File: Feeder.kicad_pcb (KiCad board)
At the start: 4 copper layers, 91 x 85 mm, 171 parts, among them J101 Conn_02x03_Odd_Even, J102 Conn_01x03_Pin, Q201 2N7002, Q301 2N7002, Q401 2N7002, Q501 2N7002, Q901 BC857BS, Q902 AO3401A, Q903 BC857BS, Q904 AO3401A, U101 XBLW 24C02S(XBLW), U201 CMP6793RE, U301 CMP6793RE, U401 LM5169PDDAR, U501 LM5169PDDAR, U601 TPS562202, U701 TPS562202, U801 CMP6793RE

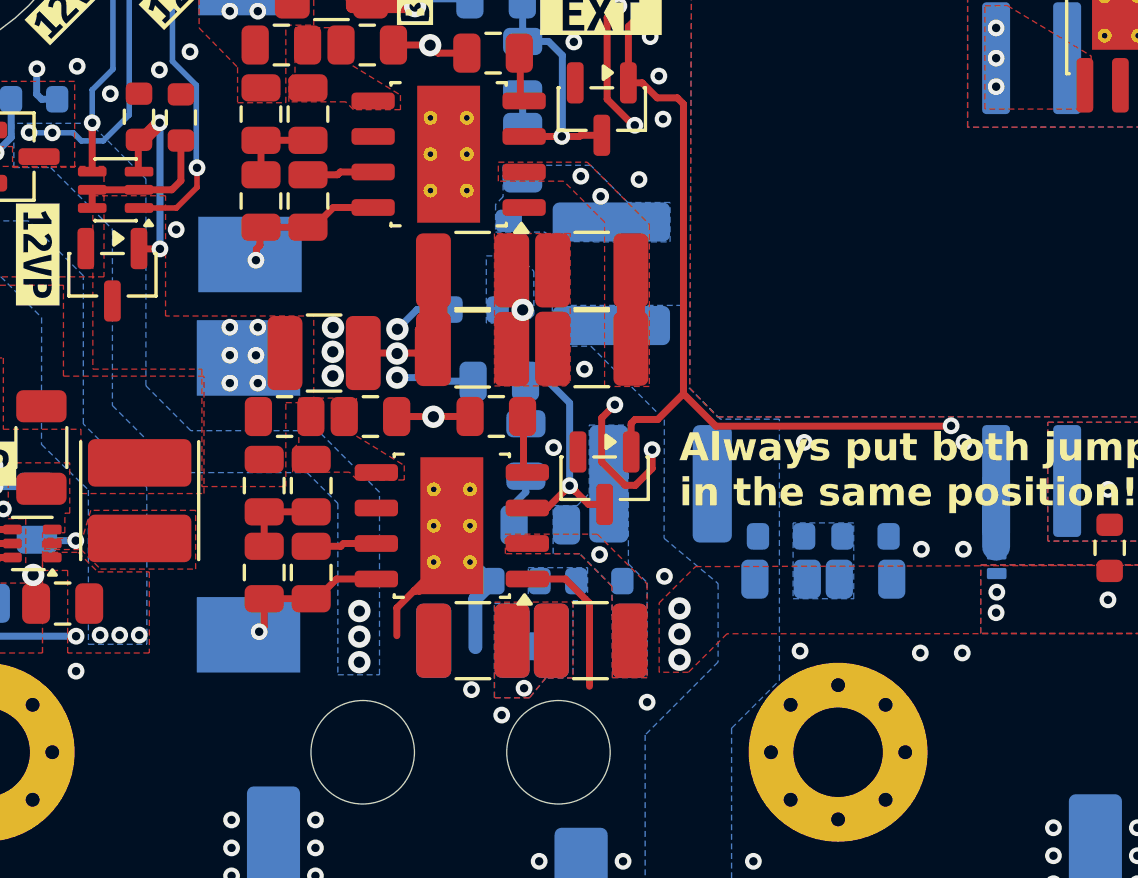
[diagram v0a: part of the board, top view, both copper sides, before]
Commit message: Updated the DRC rules so it now checks correctly B4 and A6 IPC2221 rules
Signed-off-by: Jean Alinei <jean.alinei@owntech.org>
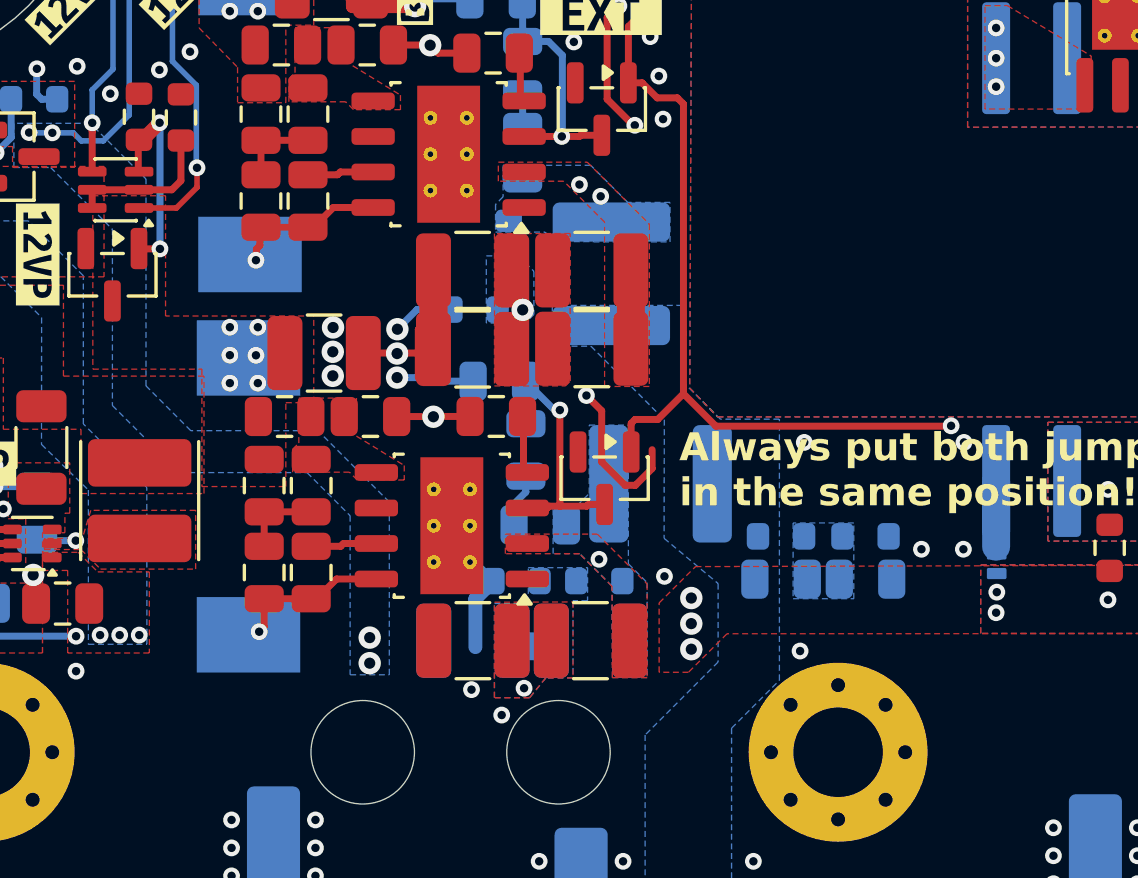
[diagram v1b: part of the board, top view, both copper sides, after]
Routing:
- net PGND: track 79.8 -> 69.0 mm, vias 165 -> 157
- net /12V_DIGI_TO_POWER: vias 14 -> 13

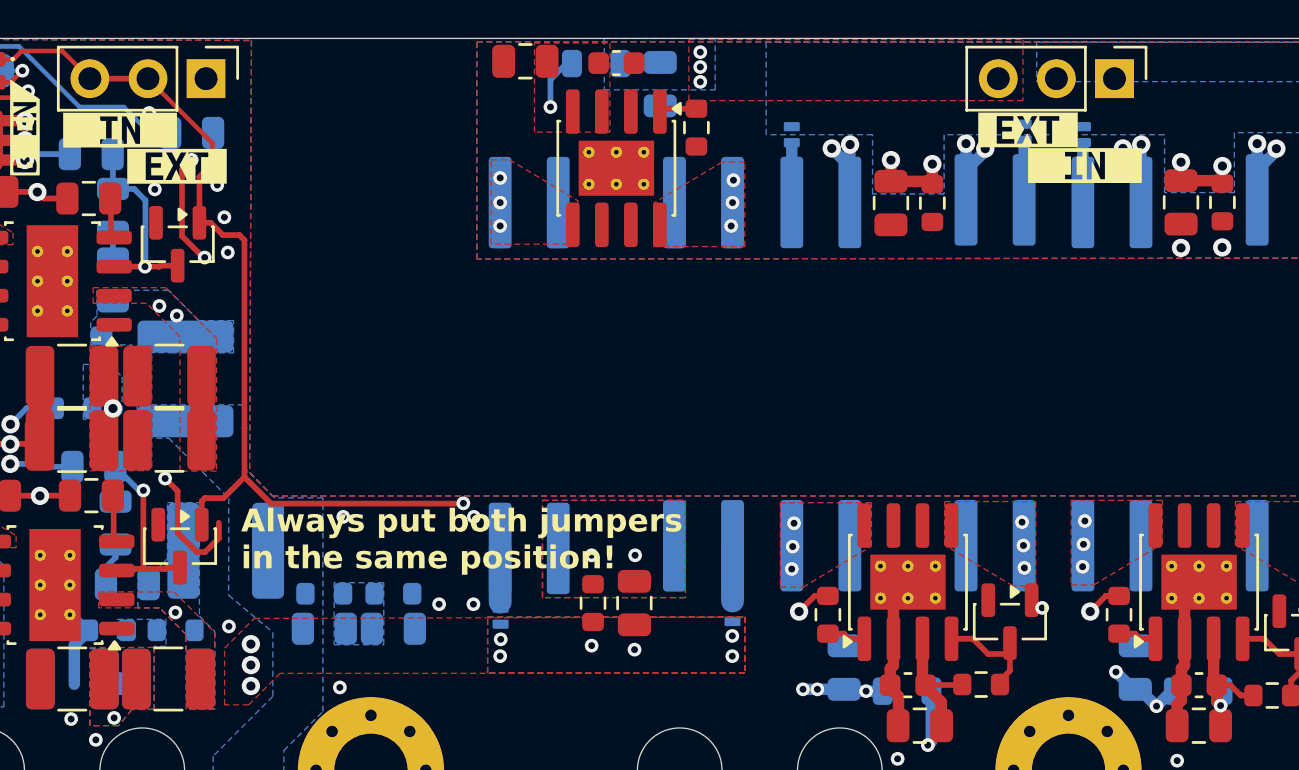
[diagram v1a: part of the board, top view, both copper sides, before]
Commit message: added y cap and changed the inductor value, added simulator of pi filter
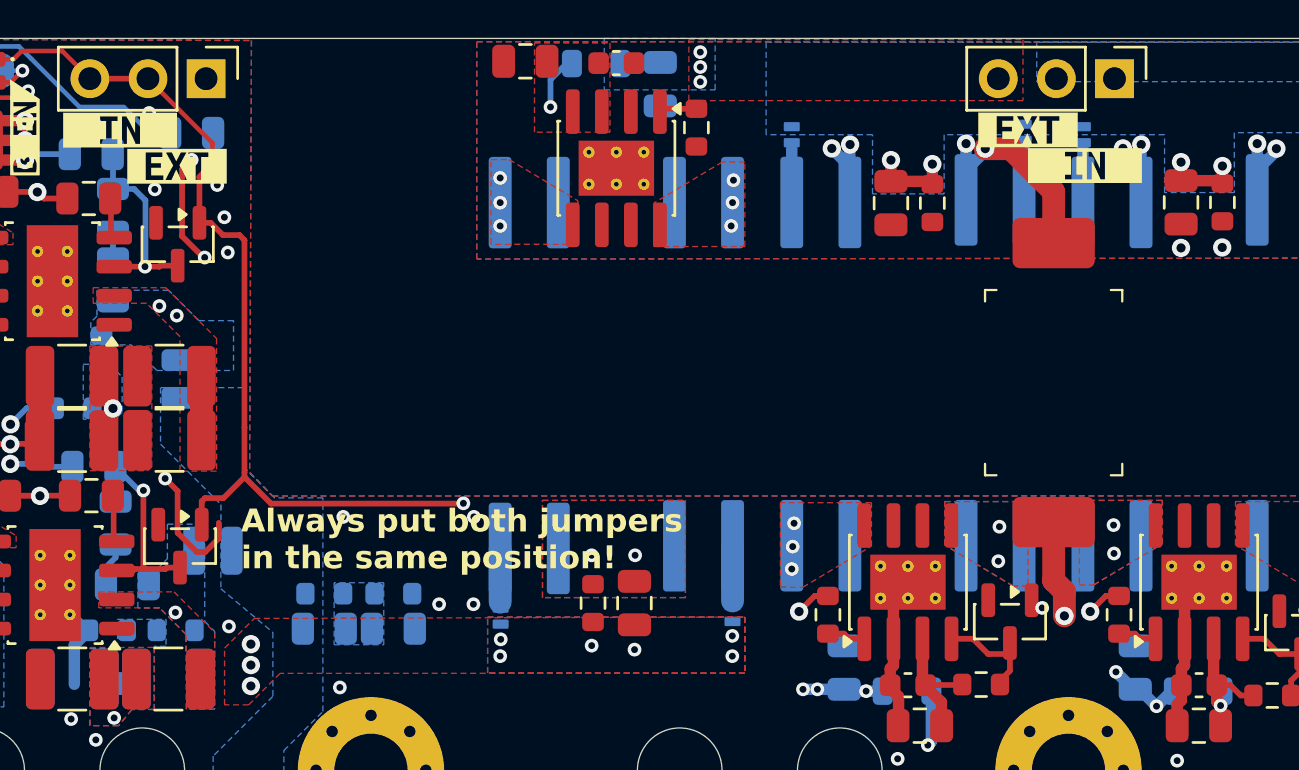
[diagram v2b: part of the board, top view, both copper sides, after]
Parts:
- added C103: 470p, Footprints:SAFETY_CAP_8.1x6mm, F.Cu at (69.1, -80.0)
- L402, L502: footprint Inductor_SMD:L_Changjiang_FNR5040S -> Inductor_SMD:L_Changjiang_FTC252008S
- moved L502 0.56 mm to (32.3, -72.6)
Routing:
- net DGND: track 30.9 -> 37.0 mm
- net PGND: track 69.0 -> 73.3 mm, vias 157 -> 158
- net Net-(U301-VD1): vias 3 -> 2
- net Net-(U201-VD2): vias 3 -> 2
- added copper zone on B.Cu, net Net-(U201-VD2)
- added copper zone on B.Cu, net Net-(U301-VD1)

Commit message: Found IC for ORing function. Added all LCSC refs. Found proper header stackup.
Signed-off-by: Jean Alinei <jean.alinei@owntech.org>
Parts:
- removed Q901, Q903: BC857BS, Package_TO_SOT_SMD:SOT-363_SC-70-6
- removed Q902, Q904: AO3401A, Package_TO_SOT_SMD:SOT-23
- removed R901, R902, R903, R904: 10k, Resistor_SMD:R_0603_1608Metric
- added C409: 22uF, Capacitor_SMD:C_0805_2012Metric, F.Cu at (15.9, -90.6)
- added C509: 22uF, Capacitor_SMD:C_0805_2012Metric, F.Cu at (20.9, -79.2)
- added U102: ~, Package_SO:SOIC-8_3.9x4.9mm_P1.27mm, F.Cu at (13.0, -85.2)
- C401, C501: value 1uF -> 2.2nF
- C402, C502: value 1uF -> 56pF
- C403, C503: value 1uF -> 3.3nF
- C404, C504: value 10uF -> 22uF; footprint Footprints:C_1210_3225Metric -> Capacitor_SMD:C_0805_2012Metric
- C405, C406, C407, C408, C505, C506, C507, C508: footprint Footprints:C_1210_3225Metric -> Capacitor_SMD:C_1206_3216Metric
- C602, C702: footprint Capacitor_SMD:C_0805_2012Metric -> Capacitor_SMD:C_0603_1608Metric
- J101: value Conn_02x03_Odd_Even -> ~; footprint Connector_PinHeader_2.54mm:PinHeader_2x03_P2.54mm_Vertical -> Footprints:PinHeader_2x03_P2.54mm_Vertical
- J102: value Conn_01x03_Pin -> ~; footprint Connector_PinHeader_2.54mm:PinHeader_1x03_P2.54mm_Vertical -> Footprints:PinHeader_1x03_P2.54mm_Vertical
- R101: value 22k -> 10K; footprint Footprints:R_0805_2012Metric -> Resistor_SMD:R_0603_1608Metric
- R401, R501, R601, R602, R701, R702: footprint Footprints:R_0805_2012Metric -> Resistor_SMD:R_0603_1608Metric
- R402, R502: value 10R -> 301k
- R403, R503: value 10R -> 453k
- R404, R504: value 38.3k -> 49.9k
- moved kibuzzard-6A746332 5.85 mm to (11.2, -78.5), turned to 0 degrees
- moved kibuzzard-6A746342 4.02 mm to (7.40, -83.2), turned to 0 degrees
- moved kibuzzard-6A746342 4.00 mm to (11.5, -81.3)
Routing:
- net Net-(Q901B-C2): track 9.03 -> 0.00 mm, vias 2 -> 0
- net Net-(Q903B-C2): track 7.50 -> 0.00 mm, vias 2 -> 0
- net /12V_PWR_BUS: track 15.4 -> 21.4 mm, vias 7 -> 6
- net Net-(Q903A-B1): track 5.39 -> 0.00 mm
- net Net-(Q901A-B1): track 3.53 -> 0.00 mm, vias 1 -> 0
- net PGND: track 73.3 -> 76.0 mm, vias 158 -> 157
- net /12V_DIGI_TO_POWER: track 12.3 -> 13.9 mm
- net +12V_PGND: track 39.0 -> 38.2 mm

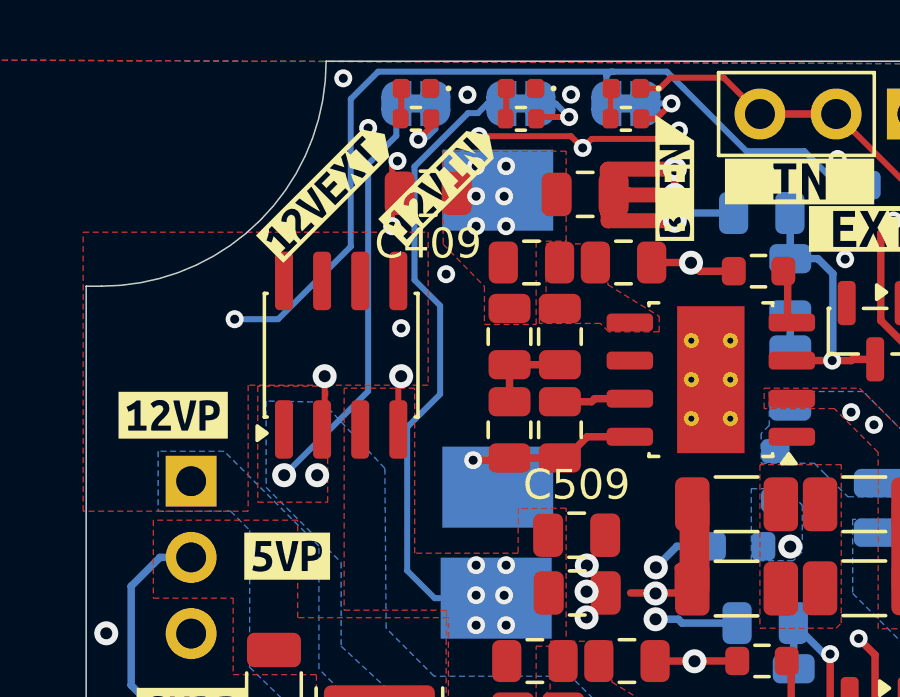
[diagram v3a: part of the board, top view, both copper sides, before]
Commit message: Added rotation offsets.
Signed-off-by: Jean Alinei <jean.alinei@owntech.org>
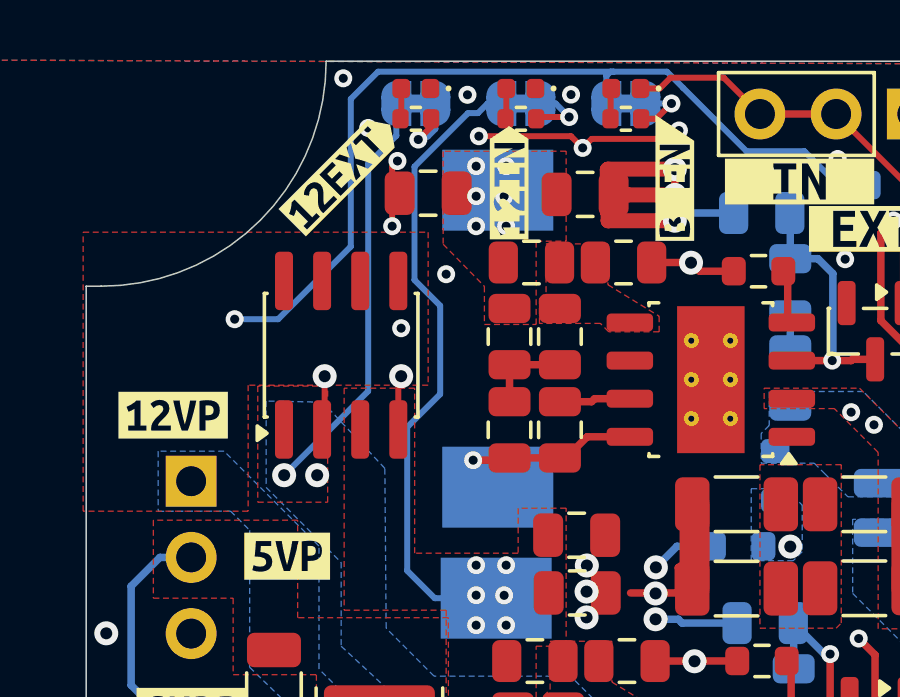
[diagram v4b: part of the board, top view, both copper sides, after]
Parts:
- removed kibuzzard-6A957F06: G***, kibuzzard-6A957F06
- removed kibuzzard-6A957F58: G***, kibuzzard-6A957F58
- added kibuzzard-6A9FF992: G***, kibuzzard-6A9FF992, F.Cu at (18.6, -91.0)
- added kibuzzard-6A9FF9B4: G***, kibuzzard-6A9FF9B4, F.Cu at (13.0, -91.2)
- D101, D102, D103: value LED -> CT-1005UBC-P4
- D201, D202, D301, D302, D801, D802: value PMEG4010 -> PMEG4010ESBYL
- J101: value ~ -> PZ254V-22-06-A60-1500
- J102: value ~ -> PZ254V-21-03-A60-1500
- U101: value XBLW 24C02S(XBLW) -> 24C02S(XBLW)
- U102: value ~ -> MX5050S3028A2
- U601, U701: value TPS562202 -> TPS562202DRLR
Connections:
- net /buck/~{EN} renamed /~{EN}
